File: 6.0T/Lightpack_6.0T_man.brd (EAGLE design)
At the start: 71 x 76.1 mm, 31 parts, among them IC1 AT90USB162, IC2 DM631_SOP24, IC3 DM631_SOP24, J1 DCJ0202, Q1 16Mhz, X1 USB-MICRO-B

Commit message: I/O names for tPlace added and rearranged.
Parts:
- removed Q1: 16Mhz, crystal:HC49UP
- added CN1: USB-MICRO-B, _USB_sockets:USB-MICRO-B-5F
- X1: value USB-MICRO-B -> 16Mhz; device _USB_sockets:USB-MICRO-B-5F -> crystal:HC49UP
- moved X1 18.7 mm to (23.2, 27.8), turned to 0 degrees
- renumbered BOOTLOADER to S1, U$1 to CN2, U$2 to CN3
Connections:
- net +5V: now also CN1.VCC; no longer X1.VCC
- net GND: now also CN1.GND; no longer X1.GND
- net N$32: now also CN1.D-; no longer X1.D-
- net N$33: now also CN1.D+; no longer X1.D+
- net N$44: now also CN1.P$7; no longer X1.P$7
- net XTAL1: now also X1.1; no longer Q1.1
- net XTAL2: now also X1.2; no longer Q1.2
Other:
- board text added: "CN1"
- board text added: "J1"
- board text added: "S1"
- board text added: "X1"

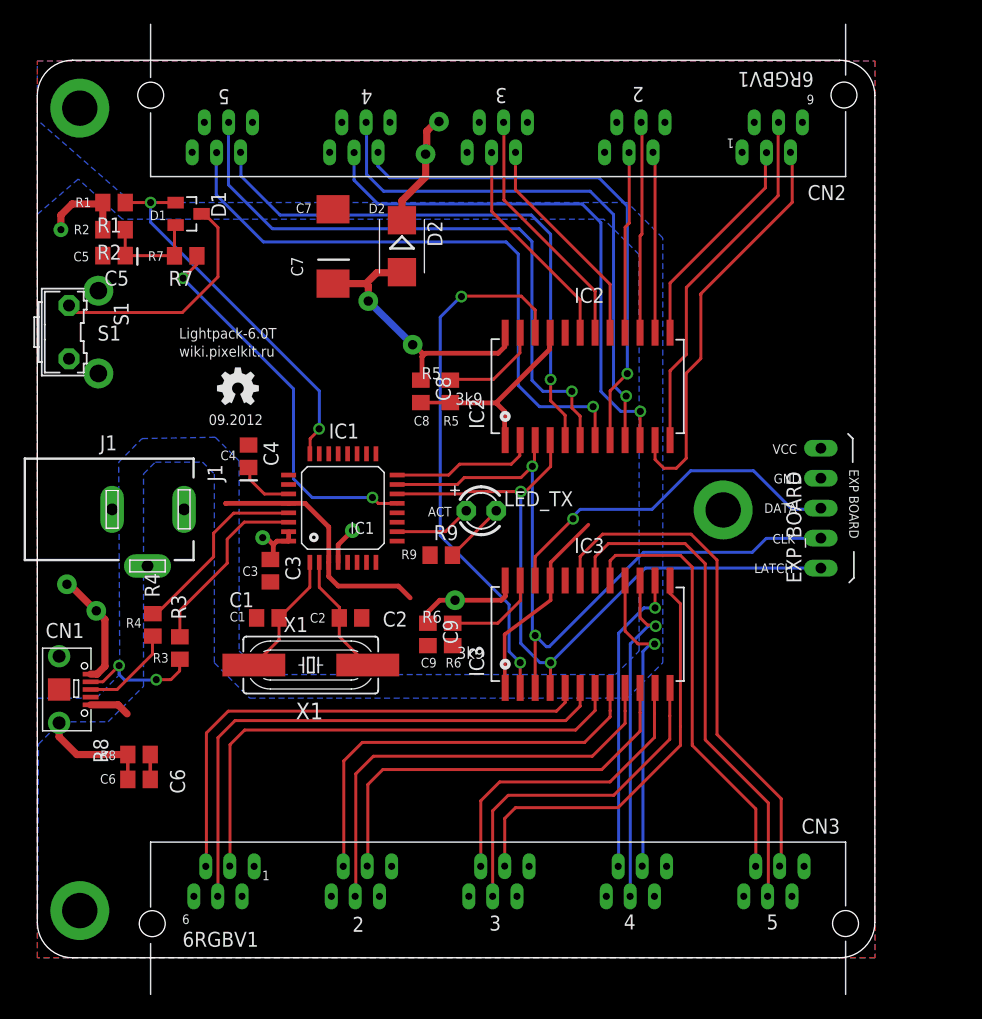
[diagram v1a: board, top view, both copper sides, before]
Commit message: Extended 78x78 version
*Mount holes fixed
*Dimensions fixed
*Polylines fixed
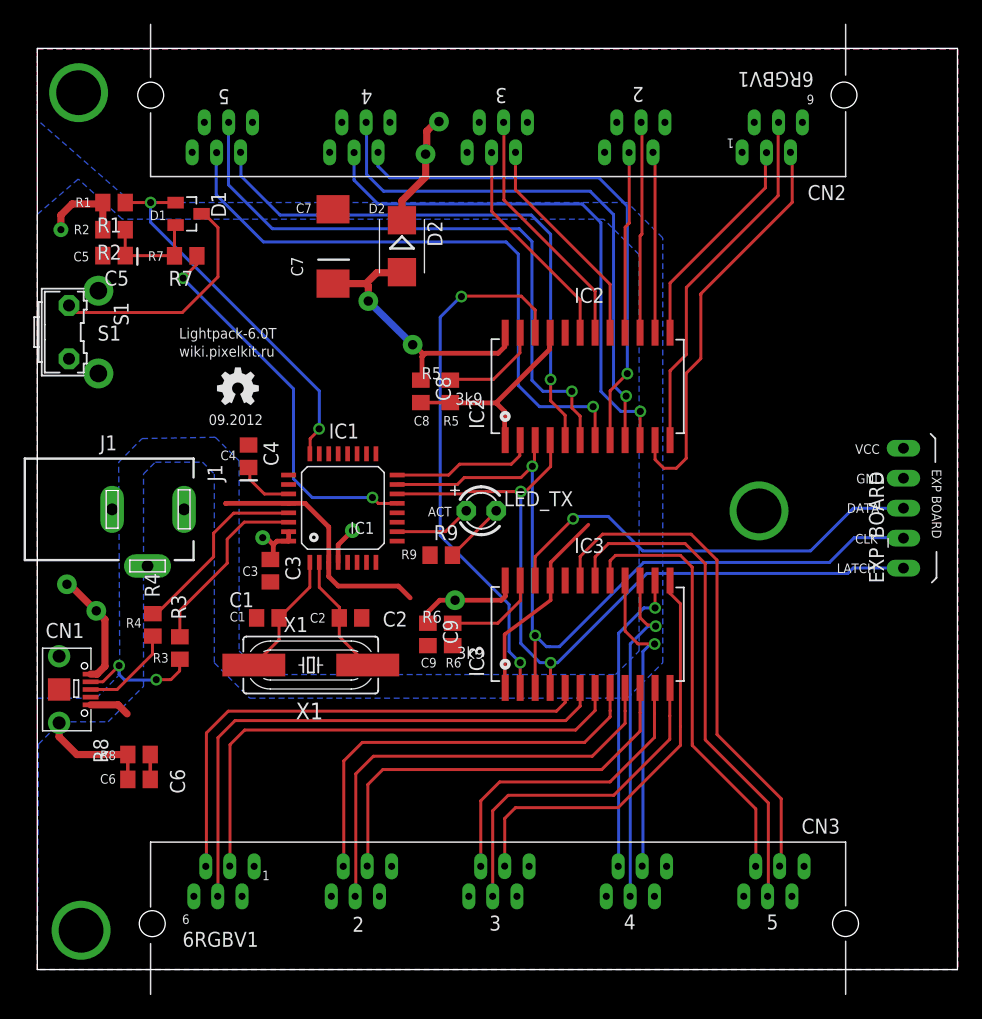
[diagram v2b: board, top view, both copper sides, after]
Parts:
- moved EXP_BOARD 7.00 mm to (73.4, 41.1)
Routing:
- net CLK: track 62.6 -> 69.7 mm
- net LATCH: track 62.3 -> 69.3 mm
- net DATA3: track 30.9 -> 37.5 mm
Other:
- board size 71 x 76.1 mm -> 78 x 78.1 mm
